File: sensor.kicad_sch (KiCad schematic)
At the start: 278 parts, among them U1 Hall_Sensor, U10 Hall_Sensor, U11 Hall_Sensor, U12 Hall_Sensor, U13 Hall_Sensor, U14 Hall_Sensor, U15 Hall_Sensor, U16 Hall_Sensor, U17 Hall_Sensor, U18 Hall_Sensor, U19 Hall_Sensor, U2 Hall_Sensor, U20 Hall_Sensor, U21 Hall_Sensor, U22 Hall_Sensor, U23 Hall_Sensor, U24 Hall_Sensor, U25 Hall_Sensor, U26 Hall_Sensor, U27 Hall_Sensor, U28 Hall_Sensor, U29 Hall_Sensor, U3 Hall_Sensor, U30 Hall_Sensor, U31 Hall_Sensor, U32 Hall_Sensor, U33 Hall_Sensor, U34 Hall_Sensor, U35 Hall_Sensor, U36 Hall_Sensor, U37 Hall_Sensor, U38 Hall_Sensor, U39 Hall_Sensor, U4 Hall_Sensor, U40 Hall_Sensor, U41 Hall_Sensor, U42 Hall_Sensor, U43 Hall_Sensor, U44 Hall_Sensor, U45 Hall_Sensor, U46 Hall_Sensor, U47 Hall_Sensor, U48 Hall_Sensor, U49 Hall_Sensor, U5 Hall_Sensor, U50 Hall_Sensor, U51 Hall_Sensor, U52 Hall_Sensor, U53 Hall_Sensor, U54 Hall_Sensor, U55 Hall_Sensor, U56 Hall_Sensor, U57 Hall_Sensor, U58 Hall_Sensor, U59 Hall_Sensor, U6 Hall_Sensor, U60 Hall_Sensor, U61 Hall_Sensor, U62 Hall_Sensor, U63 Hall_Sensor, U64 Hall_Sensor, U65 Hall_Sensor, U66 Hall_Sensor, U7 Hall_Sensor, U8 Hall_Sensor, U9 Hall_Sensor

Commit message: Second Commit
new wiring and label
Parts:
- removed AM0:0 (x2): L Alt, HE_Keyswitch:MX_Gateron_HE_1.25u, symbol voidswitch:VoidSwitch
- removed AM0:1 (x2): Z, HE_Keyswitch:MX_Gateron_HE_1u, symbol voidswitch:VoidSwitch
- removed AM0:10 (x2): Esc ` ~, HE_Keyswitch:MX_Gateron_HE_1u, symbol voidswitch:VoidSwitch
- removed AM0:11 (x2): Tab, HE_Keyswitch:MX_Gateron_HE_1.5u, symbol voidswitch:VoidSwitch
- removed AM0:12 (x2): Caps Lock, HE_Keyswitch:MX_Gateron_HE_1.75u, symbol voidswitch:VoidSwitch
- removed AM0:13 (x2): L Shift, HE_Keyswitch:MX_Gateron_HE_2.25u_Stab, symbol voidswitch:VoidSwitch
- removed AM0:14 (x2): L Ctrl, HE_Keyswitch:MX_Gateron_HE_1.25u, symbol voidswitch:VoidSwitch
- removed AM0:15 (x2): Win, HE_Keyswitch:MX_Gateron_HE_1.25u, symbol voidswitch:VoidSwitch
- removed AM0:2 (x2): A, HE_Keyswitch:MX_Gateron_HE_1u, symbol voidswitch:VoidSwitch
- removed AM0:3 (x2): S, HE_Keyswitch:MX_Gateron_HE_1u, symbol voidswitch:VoidSwitch
- removed AM0:4 (x2): E, HE_Keyswitch:MX_Gateron_HE_1u, symbol voidswitch:VoidSwitch
- removed AM0:5 (x2): 3 #, HE_Keyswitch:MX_Gateron_HE_1u, symbol voidswitch:VoidSwitch
- removed AM0:6 (x2): W, HE_Keyswitch:MX_Gateron_HE_1u, symbol voidswitch:VoidSwitch
- removed AM0:7 (x2): 2 @, HE_Keyswitch:MX_Gateron_HE_1u, symbol voidswitch:VoidSwitch
- removed AM0:8 (x2): 1 !, HE_Keyswitch:MX_Gateron_HE_1u, symbol voidswitch:VoidSwitch
- removed AM0:9 (x2): Q, HE_Keyswitch:MX_Gateron_HE_1u, symbol voidswitch:VoidSwitch
- removed AM1:0 (x2): V, HE_Keyswitch:MX_Gateron_HE_1u, symbol voidswitch:VoidSwitch
- removed AM1:1 (x2): Space, HE_Keyswitch:MX_Gateron_HE_6.25u_Stab, symbol voidswitch:VoidSwitch
- removed AM1:10 (x2): 4 $, HE_Keyswitch:MX_Gateron_HE_1u, symbol voidswitch:VoidSwitch
- removed AM1:11 (x2): D, HE_Keyswitch:MX_Gateron_HE_1u, symbol voidswitch:VoidSwitch
- removed AM1:12 (x2): X, HE_Keyswitch:MX_Gateron_HE_1u, symbol voidswitch:VoidSwitch
- removed AM1:14 (x2): C, HE_Keyswitch:MX_Gateron_HE_1u, symbol voidswitch:VoidSwitch
- removed AM1:15 (x2): F, HE_Keyswitch:MX_Gateron_HE_1u, symbol voidswitch:VoidSwitch
- removed AM1:2 (x2): G, HE_Keyswitch:MX_Gateron_HE_1u, symbol voidswitch:VoidSwitch
- removed AM1:3 (x2): B, HE_Keyswitch:MX_Gateron_HE_1u, symbol voidswitch:VoidSwitch
- removed AM1:5 (x2): Y, HE_Keyswitch:MX_Gateron_HE_1u, symbol voidswitch:VoidSwitch
- removed AM1:6 (x2): 6 ^, HE_Keyswitch:MX_Gateron_HE_1u, symbol voidswitch:VoidSwitch
- removed AM1:7 (x2): T, HE_Keyswitch:MX_Gateron_HE_1u, symbol voidswitch:VoidSwitch
- removed AM1:8 (x2): 5 %, HE_Keyswitch:MX_Gateron_HE_1u, symbol voidswitch:VoidSwitch
- removed AM1:9 (x2): R, HE_Keyswitch:MX_Gateron_HE_1u, symbol voidswitch:VoidSwitch
- removed AM2:0 (x2): M, HE_Keyswitch:MX_Gateron_HE_1u, symbol voidswitch:VoidSwitch
- removed AM2:1 (x2): , <, HE_Keyswitch:MX_Gateron_HE_1u, symbol voidswitch:VoidSwitch
- removed AM2:13 (x2): H, HE_Keyswitch:MX_Gateron_HE_1u, symbol voidswitch:VoidSwitch
- removed AM2:14 (x2): N, HE_Keyswitch:MX_Gateron_HE_1u, symbol voidswitch:VoidSwitch
- removed AM2:15 (x2): J, HE_Keyswitch:MX_Gateron_HE_1u, symbol voidswitch:VoidSwitch
- removed AM2:2 (x2): K, HE_Keyswitch:MX_Gateron_HE_1u, symbol voidswitch:VoidSwitch
- removed AM2:4 (x2): O, HE_Keyswitch:MX_Gateron_HE_1u, symbol voidswitch:VoidSwitch
- removed AM2:5 (x2): 9 (, HE_Keyswitch:MX_Gateron_HE_1u, symbol voidswitch:VoidSwitch
- removed AM2:6 (x2): I, HE_Keyswitch:MX_Gateron_HE_1u, symbol voidswitch:VoidSwitch
- removed AM2:7 (x2): 8 *, HE_Keyswitch:MX_Gateron_HE_1u, symbol voidswitch:VoidSwitch
- removed AM2:8 (x2): 7 &, HE_Keyswitch:MX_Gateron_HE_1u, symbol voidswitch:VoidSwitch
- removed AM2:9 (x2): U, HE_Keyswitch:MX_Gateron_HE_1u, symbol voidswitch:VoidSwitch
- removed AM3:0 (x2): / ?, HE_Keyswitch:MX_Gateron_HE_1u, symbol voidswitch:VoidSwitch
- removed AM3:1 (x2): Fn, HE_Keyswitch:MX_Gateron_HE_1.25u, symbol voidswitch:VoidSwitch
- removed AM3:12 (x2): L, HE_Keyswitch:MX_Gateron_HE_1u, symbol voidswitch:VoidSwitch
- removed AM3:13 (x2): . >, HE_Keyswitch:MX_Gateron_HE_1u, symbol voidswitch:VoidSwitch
- removed AM3:14 (x2): R Alt, HE_Keyswitch:MX_Gateron_HE_1.25u, symbol voidswitch:VoidSwitch
- removed AM3:15 (x2): ; :, HE_Keyswitch:MX_Gateron_HE_1u, symbol voidswitch:VoidSwitch
- removed AM3:2 (x2): ' ", HE_Keyswitch:MX_Gateron_HE_1u, symbol voidswitch:VoidSwitch
- removed AM3:4 (x2): ] }, HE_Keyswitch:MX_Gateron_HE_1u, symbol voidswitch:VoidSwitch
- removed AM3:5 (x2): = +, HE_Keyswitch:MX_Gateron_HE_1u, symbol voidswitch:VoidSwitch
- removed AM3:6 (x2): [ {, HE_Keyswitch:MX_Gateron_HE_1u, symbol voidswitch:VoidSwitch
- removed AM3:7 (x2): - _, HE_Keyswitch:MX_Gateron_HE_1u, symbol voidswitch:VoidSwitch
- removed AM3:8 (x2): 0 ), HE_Keyswitch:MX_Gateron_HE_1u, symbol voidswitch:VoidSwitch
- removed AM3:9 (x2): P, HE_Keyswitch:MX_Gateron_HE_1u, symbol voidswitch:VoidSwitch
- removed AM4:0 (x2): Right, HE_Keyswitch:MX_Gateron_HE_1u, symbol voidswitch:VoidSwitch
- removed AM4:1 (x2): PgDn End, HE_Keyswitch:MX_Gateron_HE_1u, symbol voidswitch:VoidSwitch
- removed AM4:10 (x2): Enter, HE_Keyswitch:MX_Gateron_HE_2.25u_Stab, symbol voidswitch:VoidSwitch
- removed AM4:11 (x2): R Shift, HE_Keyswitch:MX_Gateron_HE_1.75u, symbol voidswitch:VoidSwitch
- removed AM4:12 (x2): Left, HE_Keyswitch:MX_Gateron_HE_1u, symbol voidswitch:VoidSwitch
- removed AM4:14 (x2): Up, HE_Keyswitch:MX_Gateron_HE_1u, symbol voidswitch:VoidSwitch
- removed AM4:15 (x2): Down, HE_Keyswitch:MX_Gateron_HE_1u, symbol voidswitch:VoidSwitch
- removed AM4:2 (x2): PgUp Home, HE_Keyswitch:MX_Gateron_HE_1u, symbol voidswitch:VoidSwitch
- removed AM4:7 (x2): Delete Insert, HE_Keyswitch:MX_Gateron_HE_1u, symbol voidswitch:VoidSwitch
- removed AM4:8 (x2): Backspace, HE_Keyswitch:MX_Gateron_HE_2u_Stab, symbol voidswitch:VoidSwitch
- removed AM4:9 (x2): \ |, HE_Keyswitch:MX_Gateron_HE_1.5u, symbol voidswitch:VoidSwitch
- removed FID1 (x2), FID2 (x2), FID3 (x2): Fiducial, Fiducial:Fiducial_1mm_Mask2mm, symbol Mechanical:Fiducial
- removed H1 (x2), H2 (x2), H3 (x2), H4 (x2): MountingHole, MountingHole:MountingHole_3.2mm_M3_Pad, symbol Mechanical:MountingHole
- removed U1 (x2), U10 (x2), U11 (x2), U12 (x2), U13 (x2), U14 (x2), U15 (x2), U16 (x2), U17 (x2), U18 (x2), U19 (x2), U2 (x2), U20 (x2), U21 (x2), U22 (x2), U23 (x2), U24 (x2), U25 (x2), U26 (x2), U27 (x2), U28 (x2), U29 (x2), U3 (x2), U30 (x2), U31 (x2), U32 (x2), U33 (x2), U34 (x2), U35 (x2), U36 (x2), U37 (x2), U38 (x2), U39 (x2), U4 (x2), U40 (x2), U41 (x2), U42 (x2), U43 (x2), U44 (x2), U45 (x2), U46 (x2), U47 (x2), U48 (x2), U49 (x2), U5 (x2), U50 (x2), U51 (x2), U52 (x2), U53 (x2), U54 (x2), U55 (x2), U56 (x2), U57 (x2), U58 (x2), U59 (x2), U6 (x2), U60 (x2), U61 (x2), U62 (x2), U63 (x2), U64 (x2), U65 (x2), U66 (x2), U7 (x2), U8 (x2), U9 (x2): Hall_Sensor, Package_TO_SOT_SMD:SOT-23, symbol 49e:Hall_Sensor
- added AM0:0: L Alt, HE_Keyswitch:MX_Gateron_HE_1.25u, symbol voidswitch:VoidSwitch
- added AM0:1: Z, HE_Keyswitch:MX_Gateron_HE_1u, symbol voidswitch:VoidSwitch
- added AM0:10: Esc ` ~, HE_Keyswitch:MX_Gateron_HE_1u, symbol voidswitch:VoidSwitch
- added AM0:11: Tab, HE_Keyswitch:MX_Gateron_HE_1.5u, symbol voidswitch:VoidSwitch
- added AM0:12: Caps Lock, HE_Keyswitch:MX_Gateron_HE_1.75u, symbol voidswitch:VoidSwitch
- added AM0:13: L Shift, HE_Keyswitch:MX_Gateron_HE_2.25u_Stab, symbol voidswitch:VoidSwitch
- added AM0:14: L Ctrl, HE_Keyswitch:MX_Gateron_HE_1.25u, symbol voidswitch:VoidSwitch
- added AM0:15: Win, HE_Keyswitch:MX_Gateron_HE_1.25u, symbol voidswitch:VoidSwitch
- added AM0:2: A, HE_Keyswitch:MX_Gateron_HE_1u, symbol voidswitch:VoidSwitch
- added AM0:3: S, HE_Keyswitch:MX_Gateron_HE_1u, symbol voidswitch:VoidSwitch
- added AM0:4: E, HE_Keyswitch:MX_Gateron_HE_1u, symbol voidswitch:VoidSwitch
- added AM0:5: 3 #, HE_Keyswitch:MX_Gateron_HE_1u, symbol voidswitch:VoidSwitch
- added AM0:6: W, HE_Keyswitch:MX_Gateron_HE_1u, symbol voidswitch:VoidSwitch
- added AM0:7: 2 @, HE_Keyswitch:MX_Gateron_HE_1u, symbol voidswitch:VoidSwitch
- added AM0:8: 1 !, HE_Keyswitch:MX_Gateron_HE_1u, symbol voidswitch:VoidSwitch
- added AM0:9: Q, HE_Keyswitch:MX_Gateron_HE_1u, symbol voidswitch:VoidSwitch
- added AM1:0: V, HE_Keyswitch:MX_Gateron_HE_1u, symbol voidswitch:VoidSwitch
- added AM1:1: Space, HE_Keyswitch:MX_Gateron_HE_6.25u_Stab, symbol voidswitch:VoidSwitch
- added AM1:10: 4 $, HE_Keyswitch:MX_Gateron_HE_1u, symbol voidswitch:VoidSwitch
- added AM1:11: D, HE_Keyswitch:MX_Gateron_HE_1u, symbol voidswitch:VoidSwitch
- added AM1:12: X, HE_Keyswitch:MX_Gateron_HE_1u, symbol voidswitch:VoidSwitch
- added AM1:14: C, HE_Keyswitch:MX_Gateron_HE_1u, symbol voidswitch:VoidSwitch
- added AM1:15: F, HE_Keyswitch:MX_Gateron_HE_1u, symbol voidswitch:VoidSwitch
- added AM1:2: G, HE_Keyswitch:MX_Gateron_HE_1u, symbol voidswitch:VoidSwitch
- added AM1:3: B, HE_Keyswitch:MX_Gateron_HE_1u, symbol voidswitch:VoidSwitch
- added AM1:5: Y, HE_Keyswitch:MX_Gateron_HE_1u, symbol voidswitch:VoidSwitch
- added AM1:6: 6 ^, HE_Keyswitch:MX_Gateron_HE_1u, symbol voidswitch:VoidSwitch
- added AM1:7: T, HE_Keyswitch:MX_Gateron_HE_1u, symbol voidswitch:VoidSwitch
- added AM1:8: 5 %, HE_Keyswitch:MX_Gateron_HE_1u, symbol voidswitch:VoidSwitch
- added AM1:9: R, HE_Keyswitch:MX_Gateron_HE_1u, symbol voidswitch:VoidSwitch
- added AM2:0: M, HE_Keyswitch:MX_Gateron_HE_1u, symbol voidswitch:VoidSwitch
- added AM2:1: , <, HE_Keyswitch:MX_Gateron_HE_1u, symbol voidswitch:VoidSwitch
- added AM2:13: H, HE_Keyswitch:MX_Gateron_HE_1u, symbol voidswitch:VoidSwitch
- added AM2:14: N, HE_Keyswitch:MX_Gateron_HE_1u, symbol voidswitch:VoidSwitch
- added AM2:15: J, HE_Keyswitch:MX_Gateron_HE_1u, symbol voidswitch:VoidSwitch
- added AM2:2: K, HE_Keyswitch:MX_Gateron_HE_1u, symbol voidswitch:VoidSwitch
- added AM2:4: O, HE_Keyswitch:MX_Gateron_HE_1u, symbol voidswitch:VoidSwitch
- added AM2:5: 9 (, HE_Keyswitch:MX_Gateron_HE_1u, symbol voidswitch:VoidSwitch
- added AM2:6: I, HE_Keyswitch:MX_Gateron_HE_1u, symbol voidswitch:VoidSwitch
- added AM2:7: 8 *, HE_Keyswitch:MX_Gateron_HE_1u, symbol voidswitch:VoidSwitch
- added AM2:8: 7 &, HE_Keyswitch:MX_Gateron_HE_1u, symbol voidswitch:VoidSwitch
- added AM2:9: U, HE_Keyswitch:MX_Gateron_HE_1u, symbol voidswitch:VoidSwitch
- added AM3:0: / ?, HE_Keyswitch:MX_Gateron_HE_1u, symbol voidswitch:VoidSwitch
- added AM3:1: Fn, HE_Keyswitch:MX_Gateron_HE_1.25u, symbol voidswitch:VoidSwitch
- added AM3:12: L, HE_Keyswitch:MX_Gateron_HE_1u, symbol voidswitch:VoidSwitch
- added AM3:13: . >, HE_Keyswitch:MX_Gateron_HE_1u, symbol voidswitch:VoidSwitch
- added AM3:14: R Alt, HE_Keyswitch:MX_Gateron_HE_1.25u, symbol voidswitch:VoidSwitch
- added AM3:15: ; :, HE_Keyswitch:MX_Gateron_HE_1u, symbol voidswitch:VoidSwitch
- added AM3:2: ' ", HE_Keyswitch:MX_Gateron_HE_1u, symbol voidswitch:VoidSwitch
- added AM3:4: ] }, HE_Keyswitch:MX_Gateron_HE_1u, symbol voidswitch:VoidSwitch
- added AM3:5: = +, HE_Keyswitch:MX_Gateron_HE_1u, symbol voidswitch:VoidSwitch
- added AM3:6: [ {, HE_Keyswitch:MX_Gateron_HE_1u, symbol voidswitch:VoidSwitch
- added AM3:7: - _, HE_Keyswitch:MX_Gateron_HE_1u, symbol voidswitch:VoidSwitch
- added AM3:8: 0 ), HE_Keyswitch:MX_Gateron_HE_1u, symbol voidswitch:VoidSwitch
- added AM3:9: P, HE_Keyswitch:MX_Gateron_HE_1u, symbol voidswitch:VoidSwitch
- added AM4:0: Right, HE_Keyswitch:MX_Gateron_HE_1u, symbol voidswitch:VoidSwitch
- added AM4:1: PgDn End, HE_Keyswitch:MX_Gateron_HE_1u, symbol voidswitch:VoidSwitch
- added AM4:11: Enter, HE_Keyswitch:MX_Gateron_HE_2.25u_Stab, symbol voidswitch:VoidSwitch
- added AM4:12: R Shift, HE_Keyswitch:MX_Gateron_HE_1.75u, symbol voidswitch:VoidSwitch
- added AM4:13: Left, HE_Keyswitch:MX_Gateron_HE_1u, symbol voidswitch:VoidSwitch
- added AM4:14: Up, HE_Keyswitch:MX_Gateron_HE_1u, symbol voidswitch:VoidSwitch
- added AM4:15: Down, HE_Keyswitch:MX_Gateron_HE_1u, symbol voidswitch:VoidSwitch
- added AM4:2: PgUp Home, HE_Keyswitch:MX_Gateron_HE_1u, symbol voidswitch:VoidSwitch
- added AM4:7: Delete Insert, HE_Keyswitch:MX_Gateron_HE_1u, symbol voidswitch:VoidSwitch
- added AM4:8: Backspace, HE_Keyswitch:MX_Gateron_HE_2u_Stab, symbol voidswitch:VoidSwitch
- added AM4:9: \ |, HE_Keyswitch:MX_Gateron_HE_1.5u, symbol voidswitch:VoidSwitch
- added FID1, FID2, FID3: Fiducial, Fiducial:Fiducial_1mm_Mask2mm, symbol Mechanical:Fiducial
- added H1, H2, H3, H4: MountingHole, MountingHole:MountingHole_3.2mm_M3_Pad, symbol Mechanical:MountingHole
- added U1, U10, U11, U12, U13, U14, U15, U16, U17, U18, U19, U2, U20, U21, U22, U23, U24, U25, U26, U27, U28, U29, U3, U30, U31, U32, U33, U34, U35, U36, U37, U38, U39, U4, U40, U41, U42, U43, U44, U45, U46, U47, U48, U49, U5, U50, U51, U52, U53, U54, U55, U56, U57, U58, U59, U6, U60, U61, U62, U63, U64, U65, U66, U7, U8, U9: Hall_Sensor, Package_TO_SOT_SMD:SOT-23, symbol 49e:Hall_Sensor
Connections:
- net AM0:0: now also U60.2 (OUT)
- net AM0:1: now also U45.2 (OUT)
- net AM0:10: now also U1.2 (OUT)
- net AM0:11: now also U15.2 (OUT)
- net AM0:12: now also U30.2 (OUT)
- net AM0:13: now also U44.2 (OUT)
- net AM0:14: now also U58.2 (OUT)
- net AM0:15: now also U59.2 (OUT)
- net AM0:2: now also U31.2 (OUT)
- net AM0:3: now also U32.2 (OUT)
- net AM0:4: now also U18.2 (OUT)
- net AM0:5: now also U4.2 (OUT)
- net AM0:6: now also U17.2 (OUT)
- net AM0:7: now also U3.2 (OUT)
- net AM0:8: now also U2.2 (OUT)
- net AM0:9: now also U16.2 (OUT)
- net AM1:0: now also U48.2 (OUT)
- net AM1:1: now also U61.2 (OUT)
- net AM1:10: now also U5.2 (OUT)
- net AM1:11: now also U33.2 (OUT)
- net AM1:12: now also U46.2 (OUT)
- net AM1:14: now also U47.2 (OUT)
- net AM1:15: now also U34.2 (OUT)
- net AM1:2: now also U35.2 (OUT)
- net AM1:3: now also U49.2 (OUT)
- net AM1:5: now also U21.2 (OUT)
- net AM1:6: now also U7.2 (OUT)
- net AM1:7: now also U20.2 (OUT)
- net AM1:8: now also U6.2 (OUT)
- net AM1:9: now also U19.2 (OUT)
- net AM2:0: now also U51.2 (OUT)
- net AM2:1: now also U52.2 (OUT)
- net AM2:13: now also U36.2 (OUT)
- net AM2:14: now also U50.2 (OUT)
- net AM2:15: now also U37.2 (OUT)
- net AM2:2: now also U38.2 (OUT)
- net AM2:4: now also U24.2 (OUT)
- net AM2:5: now also U10.2 (OUT)
- net AM2:6: now also U23.2 (OUT)
- net AM2:7: now also U9.2 (OUT)
- net AM2:8: now also U8.2 (OUT)
- net AM2:9: now also U22.2 (OUT)
- net AM3:0: now also U54.2 (OUT)
- net AM3:1: now also U63.2 (OUT)
- net AM3:12: now also U39.2 (OUT)
- net AM3:13: now also U53.2 (OUT)
- net AM3:14: now also U62.2 (OUT)
- net AM3:15: now also U40.2 (OUT)
- net AM3:2: now also U41.2 (OUT)
- net AM3:4: now also U27.2 (OUT)
- net AM3:5: now also U13.2 (OUT)
- net AM3:6: now also U26.2 (OUT)
- net AM3:7: now also U12.2 (OUT)
- net AM3:8: now also U11.2 (OUT)
- net AM3:9: now also U25.2 (OUT)
- net AM4:0: now also U66.2 (OUT)
- net AM4:1: now also U57.2 (OUT)
- net AM4:11: now also U42.2 (OUT)
- net AM4:12: now also U55.2 (OUT)
- net AM4:14: now also U56.2 (OUT)
- net AM4:15: now also U65.2 (OUT)
- net AM4:2: now also U43.2 (OUT)
- net AM4:7: now also U29.2 (OUT)
- net AM4:8: now also U14.2 (OUT)
- net AM4:9: now also U28.2 (OUT)
- net GND: now also U1.3 (GND), U10.3 (GND), U11.3 (GND), U12.3 (GND), U13.3 (GND), U14.3 (GND), U15.3 (GND), U16.3 (GND), U17.3 (GND), U18.3 (GND), U19.3 (GND), U2.3 (GND), U20.3 (GND), U21.3 (GND), U22.3 (GND), U23.3 (GND), U24.3 (GND), U25.3 (GND), U26.3 (GND), U27.3 (GND), U28.3 (GND), U29.3 (GND), U3.3 (GND), U30.3 (GND), U31.3 (GND), U32.3 (GND), U33.3 (GND), U34.3 (GND), U35.3 (GND), U36.3 (GND), U37.3 (GND), U38.3 (GND), U39.3 (GND), U4.3 (GND), U40.3 (GND), U41.3 (GND), U42.3 (GND), U43.3 (GND), U44.3 (GND), U45.3 (GND), U46.3 (GND), U47.3 (GND), U48.3 (GND), U49.3 (GND), U5.3 (GND), U50.3 (GND), U51.3 (GND), U52.3 (GND), U53.3 (GND), U54.3 (GND), U55.3 (GND), U56.3 (GND), U57.3 (GND), U58.3 (GND), U59.3 (GND), U6.3 (GND), U60.3 (GND), U61.3 (GND), U63.3 (GND), U64.3 (GND), U65.3 (GND), U66.3 (GND), U7.3 (GND), U8.3 (GND), U9.3 (GND)
- new net 3.3V: U1.1 (VDD), U10.1 (VDD), U11.1 (VDD), U12.1 (VDD), U13.1 (VDD), U14.1 (VDD), U15.1 (VDD), U16.1 (VDD), U17.1 (VDD), U18.1 (VDD), U19.1 (VDD), U2.1 (VDD), U20.1 (VDD), U21.1 (VDD), U22.1 (VDD), U23.1 (VDD), U24.1 (VDD), U25.1 (VDD), U26.1 (VDD), U27.1 (VDD), U28.1 (VDD), U29.1 (VDD), U3.1 (VDD), U30.1 (VDD), U31.1 (VDD), U32.1 (VDD), U33.1 (VDD), U34.1 (VDD), U35.1 (VDD), U36.1 (VDD), U37.1 (VDD), U38.1 (VDD), U39.1 (VDD), U4.1 (VDD), U40.1 (VDD), U41.1 (VDD), U42.1 (VDD), U43.1 (VDD), U44.1 (VDD), U45.1 (VDD), U46.1 (VDD), U47.1 (VDD), U48.1 (VDD), U49.1 (VDD), U5.1 (VDD), U50.1 (VDD), U51.1 (VDD), U52.1 (VDD), U53.1 (VDD), U54.1 (VDD), U55.1 (VDD), U56.1 (VDD), U57.1 (VDD), U58.1 (VDD), U59.1 (VDD), U6.1 (VDD), U60.1 (VDD), U61.1 (VDD), U63.1 (VDD), U64.1 (VDD), U65.1 (VDD), U66.1 (VDD), U7.1 (VDD), U8.1 (VDD), U9.1 (VDD)
- new net AM4:13: U64.2 (OUT)

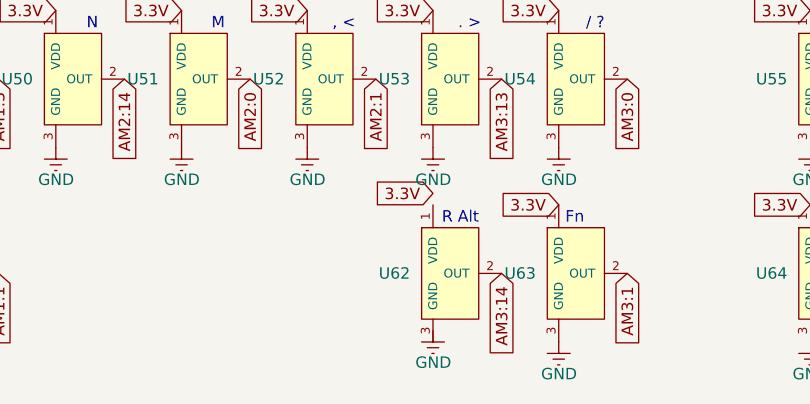
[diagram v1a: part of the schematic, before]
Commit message: Fifth Commit
updating track width and via's diameter
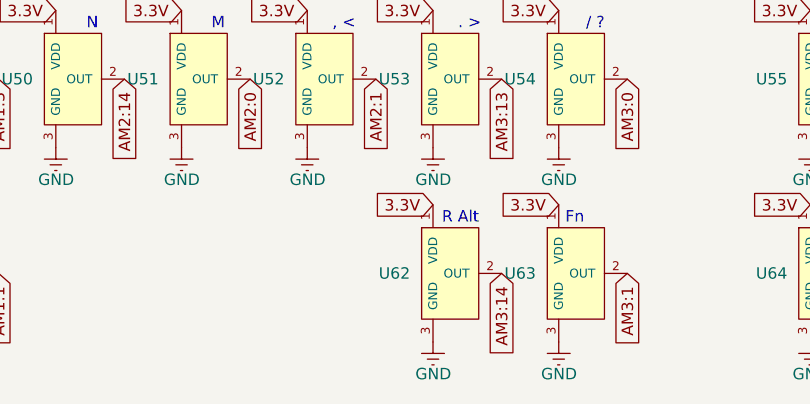
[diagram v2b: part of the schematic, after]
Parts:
- U1, U10, U11, U12, U13, U14, U15, U16, U17, U18, U19, U2, U20, U21, U22, U23, U24, U25, U26, U27, U28, U29, U3, U30, U31, U32, U33, U34, U35, U36, U37, U38, U39, U4, U40, U41, U42, U43, U44, U45, U46, U47, U48, U49, U5, U50, U51, U52, U53, U54, U55, U56, U57, U58, U59, U6, U60, U61, U62, U63, U64, U65, U66, U7, U8, U9: footprint Package_TO_SOT_SMD:SOT-23 -> HE_Keyswitch:GH39FKSW_OH49E-S
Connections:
- net 3.3V: now also U62.1 (VDD)
- net GND: now also U62.3 (GND)

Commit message: Sixth Commit
Almost done. Just need to make sure the field zone and each pin is connected properly
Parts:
- renumbered AM2:9 to AM2:8, AM2:8 to AM2:9, AM3:9 to AM3:8, AM3:8 to AM3:9
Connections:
- net AM2:8: now also U22.2 (OUT); no longer U8.2 (OUT)
- net AM2:9: now also U8.2 (OUT); no longer U22.2 (OUT)
- net AM3:8: now also U25.2 (OUT); no longer U11.2 (OUT)
- net AM3:9: now also U11.2 (OUT); no longer U25.2 (OUT)

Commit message: 7th Commit
Adding the reduced nRF52840 dongle and some minor tweak
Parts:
- H1, H2, H3, H4: footprint MountingHole:MountingHole_3.2mm_M3_Pad -> MountingHole:MountingHole_2.2mm_M2
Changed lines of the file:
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@@
 			)
 		)
-		(property "Footprint" "MountingHole:MountingHole_3.2mm_M3_Pad"
+		(property "Footprint" "MountingHole:MountingHole_2.2mm_M2"
 			(at 271.78 38.1 0)
 			(effects
@@
 			)
 		)
-		(property "Footprint" "MountingHole:MountingHole_3.2mm_M3_Pad"
+		(property "Footprint" "MountingHole:MountingHole_2.2mm_M2"
 			(at 271.78 25.4 0)
 			(effects
@@
 			)
 		)
-		(property "Footprint" "MountingHole:MountingHole_3.2mm_M3_Pad"
+		(property "Footprint" "MountingHole:MountingHole_2.2mm_M2"
 			(at 271.78 44.45 0)
 			(effects
@@
 			)
 		)
-		(property "Footprint" "MountingHole:MountingHole_3.2mm_M3_Pad"
+		(property "Footprint" "MountingHole:MountingHole_2.2mm_M2"
 			(at 271.78 31.75 0)
 			(effects
